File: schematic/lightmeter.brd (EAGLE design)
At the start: 26.7 x 38.6 mm, 91 parts, among them J1 CONNECTEDJUMPER, J2 CONNECTEDJUMPER, J3 CONNECTEDJUMPER, J4 CONNECTEDJUMPER, J5 CONNECTEDJUMPER, J6 CONNECTEDJUMPER, J7 CONNECTEDJUMPER, Q1 PCHANNELMOSFETSOT-523-3-BTTM, Y1 8MHz

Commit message: Some tweaks to layout.
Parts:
- R12: value 10k -> 10k%
- moved R13 8.68 mm to (2.64, 5.54)
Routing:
- net GND: track 177.0 -> 174.9 mm
- net I2CSDA: track 65.5 -> 64.1 mm, vias 2 -> 4
- net PBI$1: track 28.4 -> 29.7 mm
- net I2CSCL: track 60.1 -> 61.3 mm, vias 2 -> 4
- net SCRRES: track 16.0 -> 15.0 mm
- net PBI$2: track 43.6 -> 42.6 mm
- net VUSB: track 39.3 -> 39.8 mm

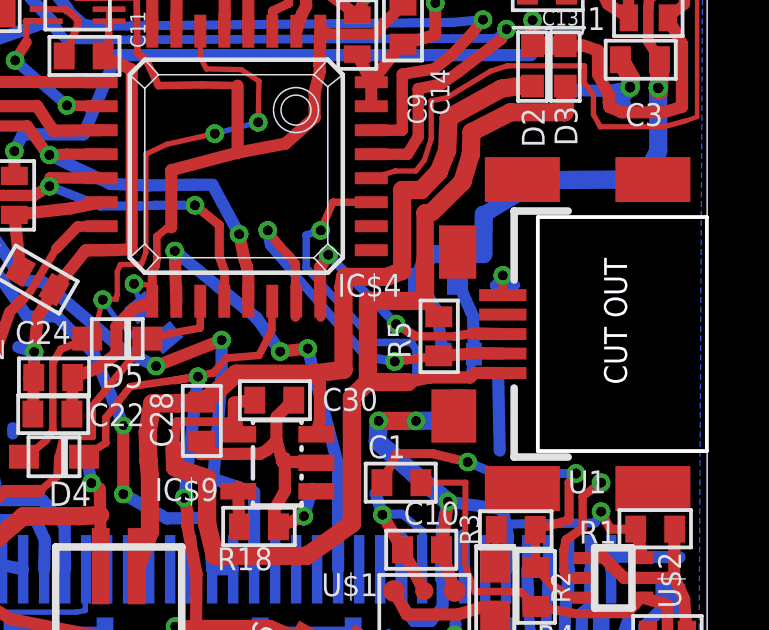
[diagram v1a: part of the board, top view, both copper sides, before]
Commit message: Fix screen power mosfet pad layout error
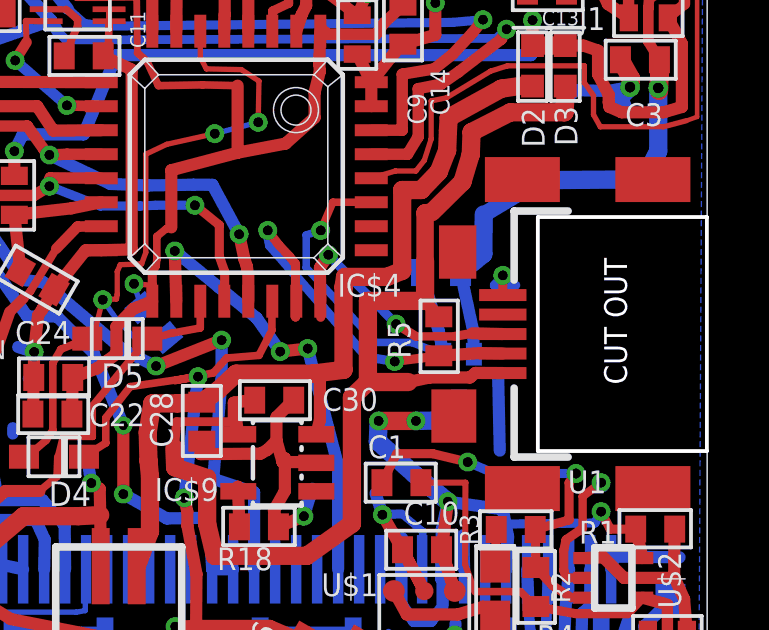
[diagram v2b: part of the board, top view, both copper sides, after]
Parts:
- moved R10 0.31 mm to (19.1, 16.9), turned to 180 degrees
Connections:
- net SCRPWR: now also Q1.P$3; no longer Q1.P$2
- net VREG: now also Q1.P$2; no longer Q1.P$3
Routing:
- net SCRPWR: track 14.8 -> 12.4 mm
- net VREG: track 82.4 -> 80.7 mm
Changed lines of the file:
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@@
 <attribute name="VALUE" x="23.9522" y="28.9369" size="0.4064" layer="27" ratio="10"/>
 </element>
-<element name="R10" library="resistor" package="R0402" value="390k" x="18.9992" y="16.64461875" smashed="yes" rot="MR0">
-<attribute name="SPICEPREFIX" value="R" x="18.9992" y="16.64461875" size="1.778" layer="28" rot="MR0" display="off"/>
-<attribute name="NAME" x="19.6342" y="17.40661875" size="0.762" layer="26" rot="MR0"/>
-<attribute name="VALUE" x="19.6342" y="14.61261875" size="1.27" layer="28" rot="MR0"/>
+<element name="R10" library="resistor" package="R0402" value="390k" x="19.1008" y="16.93418125" smashed="yes" rot="MR180">
+<attribute name="SPICEPREFIX" value="R" x="19.1008" y="16.93418125" size="1.778" layer="28" rot="MR180" display="off"/>
+<attribute name="NAME" x="18.4658" y="16.17218125" size="0.762" layer="26" rot="MR180"/>
+<attribute name="VALUE" x="18.4658" y="18.96618125" size="1.27" layer="28" rot="MR180"/>
 </element>
 <element name="R13" library="resistor" package="R0402" value="390k" x="2.6416" y="5.5372" smashed="yes" rot="MR270">
@@
 <wire x1="26.3802" y1="24.0284" x2="26.0096" y2="24.638" width="0.3556" layer="1"/>
 <wire x1="26.0096" y1="24.638" x2="26.0096" y2="25.7556" width="0.3556" layer="1"/>
-<wire x1="18.671503125" y1="17.5514" x2="20.5088" y2="17.5514" width="0.6096" layer="16"/>
 <wire x1="20.5088" y1="17.5514" x2="20.5232" y2="18.8722" width="0.6096" layer="16"/>
-<wire x1="18.3492" y1="16.64461875" x2="18.671503125" y2="17.5514" width="0.6096" layer="16"/>
 <contactref element="C24" pad="1"/>
 <wire x1="6.8222" y1="13.4366" x2="7.6348" y2="13.7414" width="0.4064" layer="1"/>
@@
 <wire x1="7.471746875" y1="28.85948125" x2="7.8636" y2="29.69768125" width="0.2286" layer="1"/>
 <wire x1="7.6858" y1="27.8534" x2="7.508" y2="28.067" width="0.2286" layer="1"/>
-<contactref element="Q1" pad="P$3"/>
-<wire x1="19.174459375" y1="14.2113" x2="18.9484" y2="15.6718" width="0.4064" layer="16"/>
-<wire x1="18.9484" y1="15.6718" x2="18.3492" y2="16.64461875" width="0.4064" layer="16"/>
+<contactref element="Q1" pad="P$2"/>
 <wire x1="26.6573" y1="26.4541" x2="26.6573" y2="28.4734" width="0.4064" layer="1"/>
 <wire x1="26.6573" y1="28.4734" x2="25.9944" y2="29.3694" width="0.4064" layer="1"/>
@@
 <wire x1="21.336" y1="30.3784" x2="22.098" y2="30.1244" width="0.4064" layer="1"/>
 <wire x1="22.098" y1="30.1244" x2="22.098" y2="28.3718" width="0.4064" layer="1"/>
+<wire x1="19.7508" y1="16.93418125" x2="20.1676" y2="15.0114" width="0.4064" layer="16"/>
+<wire x1="20.1676" y1="15.0114" x2="20.195540625" y2="14.2113" width="0.4064" layer="16"/>
+<wire x1="20.5088" y1="17.5514" x2="19.7508" y2="16.93418125" width="0.6096" layer="16"/>
 </signal>
 <signal name="N$19">
@@
 <signal name="SCRPWR">
 <contactref element="R10" pad="1"/>
-<contactref element="Q1" pad="P$2"/>
-<wire x1="20.195540625" y1="14.2113" x2="20.1676" y2="15.4686" width="0.4064" layer="16"/>
-<wire x1="20.1676" y1="15.4686" x2="19.6492" y2="16.64461875" width="0.4064" layer="16"/>
-<wire x1="18.4658" y1="13.3096" x2="18.8722" y2="13.4366" width="0.254" layer="16"/>
-<wire x1="18.8722" y1="13.4366" x2="20.0152" y2="13.4366" width="0.254" layer="16"/>
-<wire x1="20.0152" y1="13.4366" x2="20.195540625" y2="14.2113" width="0.254" layer="16"/>
+<contactref element="Q1" pad="P$3"/>
 <contactref element="IC$4" pad="27"/>
 <wire x1="15.494" y1="19.2786" x2="16.7746" y2="19.2788" width="0.254" layer="1"/>
-<wire x1="18.4658" y1="13.3096" x2="18.2626" y2="13.5636" width="0.254" layer="16"/>
-<wire x1="18.2626" y1="13.5636" x2="18.2626" y2="14.3764" width="0.254" layer="16"/>
-<wire x1="18.2626" y1="14.3764" x2="18.1102" y2="14.605" width="0.254" layer="16"/>
 <wire x1="18.1102" y1="14.605" x2="16.9164" y2="14.605" width="0.254" layer="16"/>
 <wire x1="16.9164" y1="14.605" x2="14.605" y2="17.0942" width="0.254" layer="16"/>
@@
 <via x="15.0876" y="18.3388" extent="1-16" drill="0.3302" shape="square"/>
 <wire x1="15.0876" y1="18.3388" x2="15.494" y2="19.2786" width="0.254" layer="1"/>
+<wire x1="18.4508" y1="16.93418125" x2="19.0246" y2="14.986" width="0.4064" layer="16"/>
+<wire x1="19.0246" y1="14.986" x2="19.174459375" y2="14.2113" width="0.4064" layer="16"/>
+<wire x1="18.1102" y1="14.605" x2="19.174459375" y2="14.2113" width="0.254" layer="16"/>
 </signal>
 <signal name="PBI$1">

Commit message: Minor updates to schematic.
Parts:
- C2: value 3300p -> 3300p (1%)
- C20, C21: value 3300p% -> 3300p (1%)
- R11: value 10k% -> 10k (0.1%)
- R12: value 10k% -> 10k (0.1%
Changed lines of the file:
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@@
 <attribute name="VALUE" x="7.8232" y="26.0604" size="1.27" layer="27" rot="R180"/>
 </element>
-<element name="C20" library="rcl" package="C0603" value="3300p%" x="15.5956" y="31.242" smashed="yes" rot="R270">
+<element name="C20" library="rcl" package="C0603" value="3300p (1%)" x="15.5956" y="31.242" smashed="yes" rot="R270">
 <attribute name="NAME" x="14.7828" y="30.099" size="0.762" layer="25" rot="R90"/>
 <attribute name="VALUE" x="13.6906" y="31.877" size="1.27" layer="27" rot="R270"/>
 </element>
-<element name="C21" library="rcl" package="C0603" value="3300p%" x="5.6388" y="32.11321875" smashed="yes" rot="R270">
+<element name="C21" library="rcl" package="C0603" value="3300p (1%)" x="5.6388" y="32.11321875" smashed="yes" rot="R270">
 <attribute name="NAME" x="7.1882" y="31.40201875" size="0.762" layer="25" rot="R90"/>
 <attribute name="VALUE" x="3.7338" y="32.74821875" size="1.27" layer="27" rot="R270"/>
@@
 <attribute name="VALUE" x="19.623009375" y="35.83873125" size="1.27" layer="27" rot="R165"/>
 </element>
-<element name="R11" library="resistor" package="R0402" value="10k%" x="16.9926" y="31.4198" smashed="yes" rot="R90">
+<element name="R11" library="resistor" package="R0402" value="10k (0.1%)" x="16.9926" y="31.4198" smashed="yes" rot="R90">
 <attribute name="SPICEPREFIX" value="R" x="16.9926" y="31.4198" size="1.778" layer="27" rot="R90" display="off"/>
 <attribute name="NAME" x="19.5326" y="32.893" size="0.762" layer="25" rot="R180"/>
@@
 <attribute name="VALUE" x="13.6652" y="26.67" size="1.27" layer="27"/>
 </element>
-<element name="R12" library="resistor" package="R0402" value="10k%" x="4.445" y="32.1056" smashed="yes" rot="R90">
+<element name="R12" library="resistor" package="R0402" value="10k (0.1%" x="4.445" y="32.1056" smashed="yes" rot="R90">
 <attribute name="SPICEPREFIX" value="R" x="4.445" y="32.1056" size="1.778" layer="27" rot="R90" display="off"/>
 <attribute name="NAME" x="3.6322" y="30.7086" size="0.762" layer="25" rot="R90"/>
@@
 <attribute name="VALUE" x="11.7602" y="30.3784" size="1.27" layer="27" rot="R180"/>
 </element>
-<element name="C2" library="rcl" package="C0603" value="3300p" x="20.9042" y="6.2992" smashed="yes" rot="R90">
+<element name="C2" library="rcl" package="C0603" value="3300p (1%)" x="20.9042" y="6.2992" smashed="yes" rot="R90">
 <attribute name="NAME" x="21.4122" y="3.7592" size="0.635" layer="25" rot="R90"/>
 <attribute name="VALUE" x="22.8092" y="5.6642" size="1.27" layer="27" rot="R90"/>

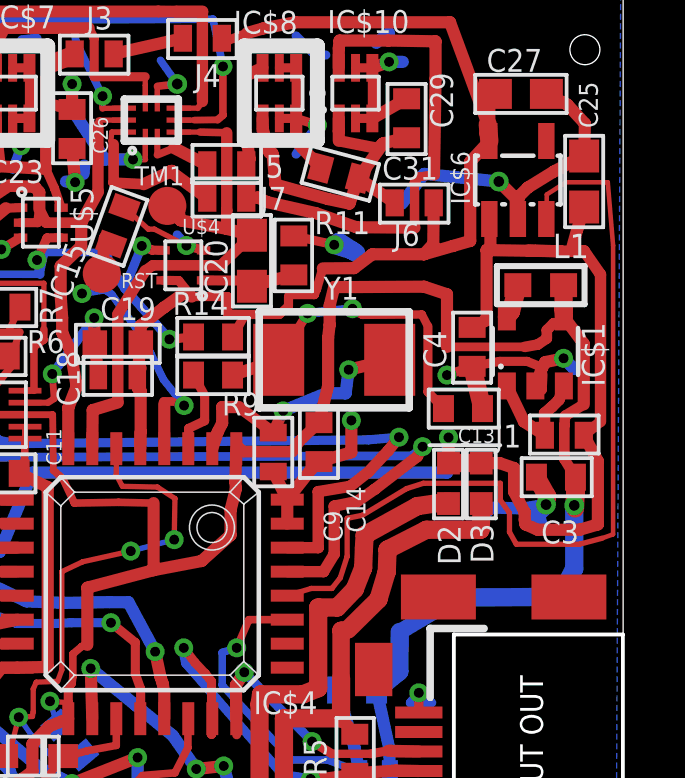
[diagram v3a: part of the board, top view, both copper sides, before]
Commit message: Get rid of LREGENABLE (STM32 needs AVDD to be high to start up)
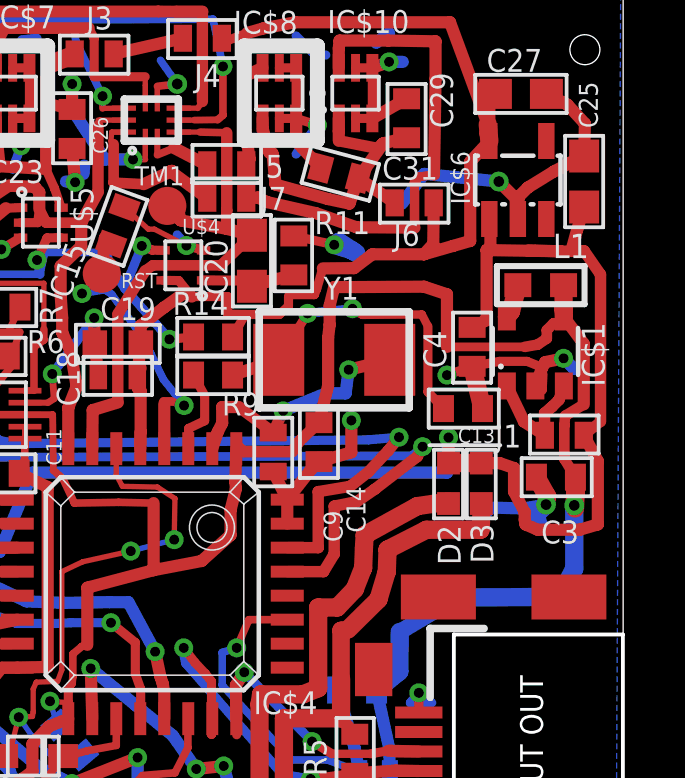
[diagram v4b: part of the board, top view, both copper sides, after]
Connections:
- removed net LREGENABLE: IC$4.28, IC$6.3
- net VCC: now also IC$6.3
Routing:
- net LREGENABLE: track 29.6 -> 0.00 mm
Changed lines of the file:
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@@
 <contactref element="R16" pad="1"/>
 <wire x1="4.8768" y1="20.1572" x2="4.8768" y2="20.9804" width="0.4064" layer="1"/>
+<contactref element="IC$6" pad="3"/>
+<wire x1="26.4412" y1="32.2938" x2="25.4102" y2="32.6344" width="0" layer="19" extent="1-1"/>
 </signal>
 <signal name="VREG">
@@
 <wire x1="14.605" y1="2.667" x2="15.2988" y2="2.842371875" width="0.4064" layer="1"/>
 </signal>
-<signal name="LREGENABLE">
-<contactref element="IC$6" pad="3"/>
-<contactref element="IC$4" pad="28"/>
-<wire x1="27.6352" y1="31.75" x2="27.6352" y2="22.1234" width="0.1524" layer="1"/>
-<wire x1="27.6352" y1="22.1234" x2="27.2796" y2="21.9964" width="0.1524" layer="1"/>
-<wire x1="27.2796" y1="21.9964" x2="26.5176" y2="21.7932" width="0.1778" layer="1"/>
-<wire x1="26.5176" y1="21.7932" x2="24.4094" y2="21.7932" width="0.1778" layer="1"/>
-<wire x1="16.7746" y1="20.0788" x2="17.5768" y2="20.32" width="0.1778" layer="1"/>
-<wire x1="17.5768" y1="20.32" x2="18.2626" y2="20.32" width="0.1778" layer="1"/>
-<wire x1="18.2626" y1="20.32" x2="18.542" y2="20.6756" width="0.1778" layer="1"/>
-<wire x1="18.542" y1="20.6756" x2="18.7706" y2="21.3868" width="0.1778" layer="1"/>
-<wire x1="18.7706" y1="21.3868" x2="18.7706" y2="22.6568" width="0.1778" layer="1"/>
-<wire x1="18.7706" y1="22.6568" x2="19.2786" y2="22.7584" width="0.1778" layer="1"/>
-<wire x1="19.2786" y1="22.7584" x2="20.7518" y2="23.6474" width="0.1778" layer="1"/>
-<wire x1="20.7518" y1="23.6474" x2="21.3106" y2="23.8252" width="0.1778" layer="1"/>
-<wire x1="21.3106" y1="23.8252" x2="23.876" y2="23.8252" width="0.1778" layer="1"/>
-<wire x1="23.876" y1="23.8252" x2="23.876" y2="23.2664" width="0.1778" layer="1"/>
-<wire x1="23.876" y1="23.2664" x2="24.1808" y2="22.8346" width="0.1778" layer="1"/>
-<wire x1="24.1808" y1="22.8346" x2="24.1808" y2="22.1996" width="0.1778" layer="1"/>
-<wire x1="24.1808" y1="22.1996" x2="24.4094" y2="21.7932" width="0.1778" layer="1"/>
-<wire x1="27.6352" y1="31.75" x2="27.4574" y2="33.8582" width="0.1524" layer="1"/>
-<wire x1="27.4574" y1="33.8582" x2="26.0604" y2="33.8582" width="0.1524" layer="1"/>
-<wire x1="26.0604" y1="33.8582" x2="25.4254" y2="33.4518" width="0.1524" layer="1"/>
-<wire x1="25.4254" y1="33.4518" x2="25.4102" y2="32.6344" width="0.1524" layer="1"/>
-</signal>
 <signal name="ACCELINT2">

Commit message: Some progress on metering mess.
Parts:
- R11: value 10k (0.1%) -> 500 (0.1%)
- R12: value 10k (0.1% -> 500 (0.1%
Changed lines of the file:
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@@
 <attribute name="VALUE" x="19.623009375" y="35.83873125" size="1.27" layer="27" rot="R165"/>
 </element>
-<element name="R11" library="resistor" package="R0402" value="10k (0.1%)" x="16.9926" y="31.4198" smashed="yes" rot="R90">
+<element name="R11" library="resistor" package="R0402" value="500 (0.1%)" x="16.9926" y="31.4198" smashed="yes" rot="R90">
 <attribute name="SPICEPREFIX" value="R" x="16.9926" y="31.4198" size="1.778" layer="27" rot="R90" display="off"/>
 <attribute name="NAME" x="19.5326" y="32.893" size="0.762" layer="25" rot="R180"/>
@@
 <attribute name="VALUE" x="13.6652" y="26.67" size="1.27" layer="27"/>
 </element>
-<element name="R12" library="resistor" package="R0402" value="10k (0.1%" x="4.445" y="32.1056" smashed="yes" rot="R90">
+<element name="R12" library="resistor" package="R0402" value="500 (0.1%" x="4.445" y="32.1056" smashed="yes" rot="R90">
 <attribute name="SPICEPREFIX" value="R" x="4.445" y="32.1056" size="1.778" layer="27" rot="R90" display="off"/>
 <attribute name="NAME" x="3.6322" y="30.7086" size="0.762" layer="25" rot="R90"/>

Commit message: Is it finally fixed (??)
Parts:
- R12: value 500 (0.1% -> 500 (0.1%)
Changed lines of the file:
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@@
 <attribute name="VALUE" x="13.6652" y="26.67" size="1.27" layer="27"/>
 </element>
-<element name="R12" library="resistor" package="R0402" value="500 (0.1%" x="4.445" y="32.1056" smashed="yes" rot="R90">
+<element name="R12" library="resistor" package="R0402" value="500 (0.1%)" x="4.445" y="32.1056" smashed="yes" rot="R90">
 <attribute name="SPICEPREFIX" value="R" x="4.445" y="32.1056" size="1.778" layer="27" rot="R90" display="off"/>
 <attribute name="NAME" x="3.6322" y="30.7086" size="0.762" layer="25" rot="R90"/>

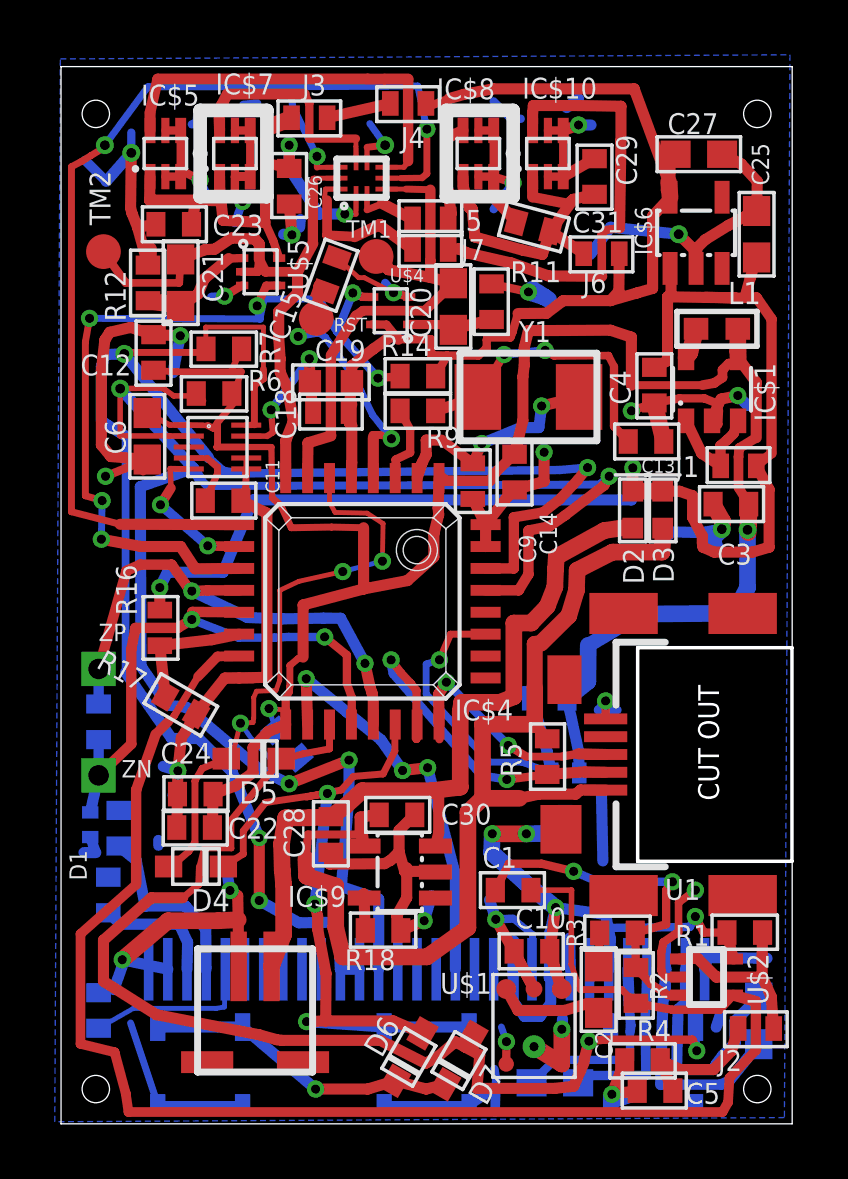
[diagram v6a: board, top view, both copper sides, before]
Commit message: Some improvements to ground plane connectivity.
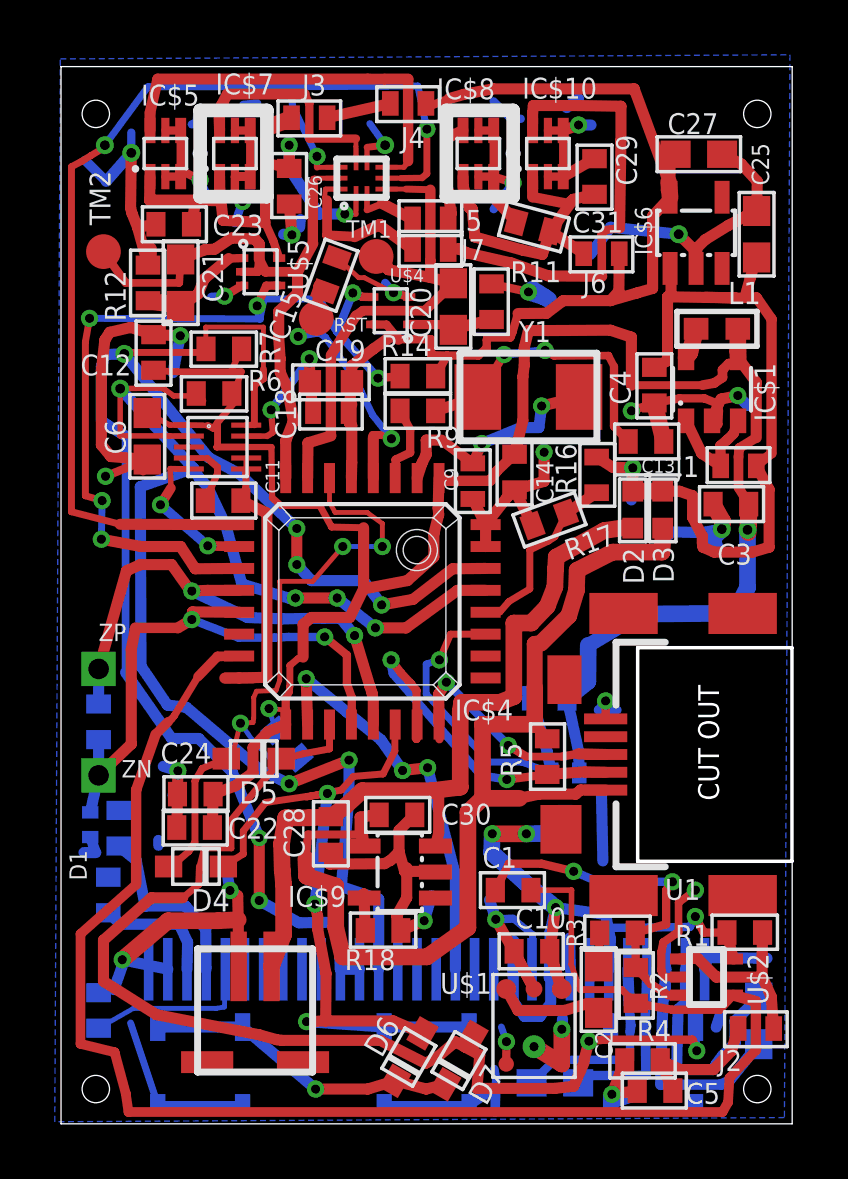
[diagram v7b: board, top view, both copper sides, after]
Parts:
- moved R16 16.9 mm to (20.8, 25.1)
- moved R17 15.1 mm to (19.1, 23.5), turned to 200 degrees
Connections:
- net BATVOLTAGE: now also IC$4.28; no longer IC$4.14
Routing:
- net VCC: track 48.8 -> 30.0 mm, vias 2 -> 1
- net I2CSCL: track 61.3 -> 53.0 mm, vias 4 -> 6
- net I2CSDA: track 64.1 -> 57.2 mm, vias 4 -> 6
- net GND: track 174.9 -> 172.4 mm
- net BATVOLTAGE: track 4.79 -> 6.67 mm
